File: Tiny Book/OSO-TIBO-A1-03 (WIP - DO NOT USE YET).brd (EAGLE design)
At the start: 54.9 x 88.1 mm, 106 parts, among them J2 10118193-0001LF, Q1 DMG341, Q2 IRLML0100, SW2 SPDT_SWITCH, U1 AP2112-3.3, U2 MCP73831T-2ACI/OT, U3 ATSAMD51G18A-MUT, U4 GD25Q32C, U5 MAX4468EKAT, X1 JSTPH, X2 2x5 0.05" SWD

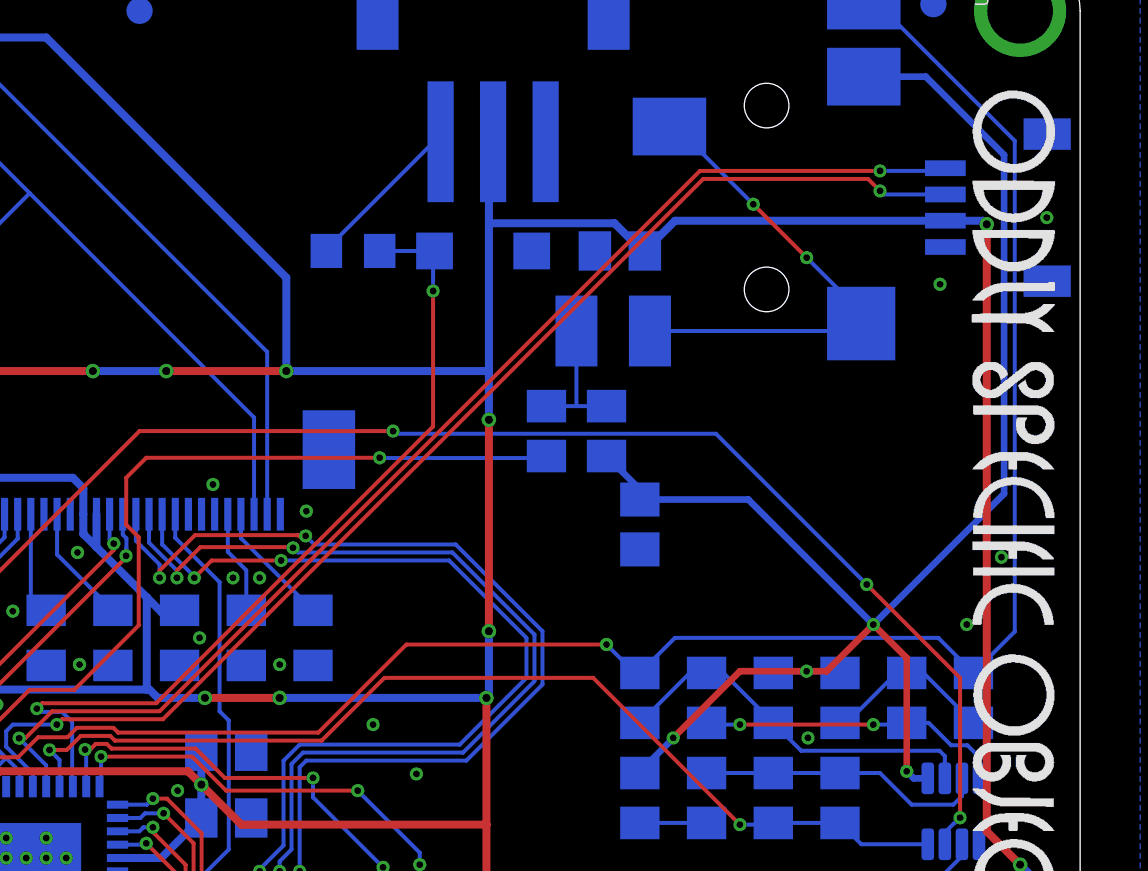
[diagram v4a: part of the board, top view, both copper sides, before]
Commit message: fix I2C routing snafu
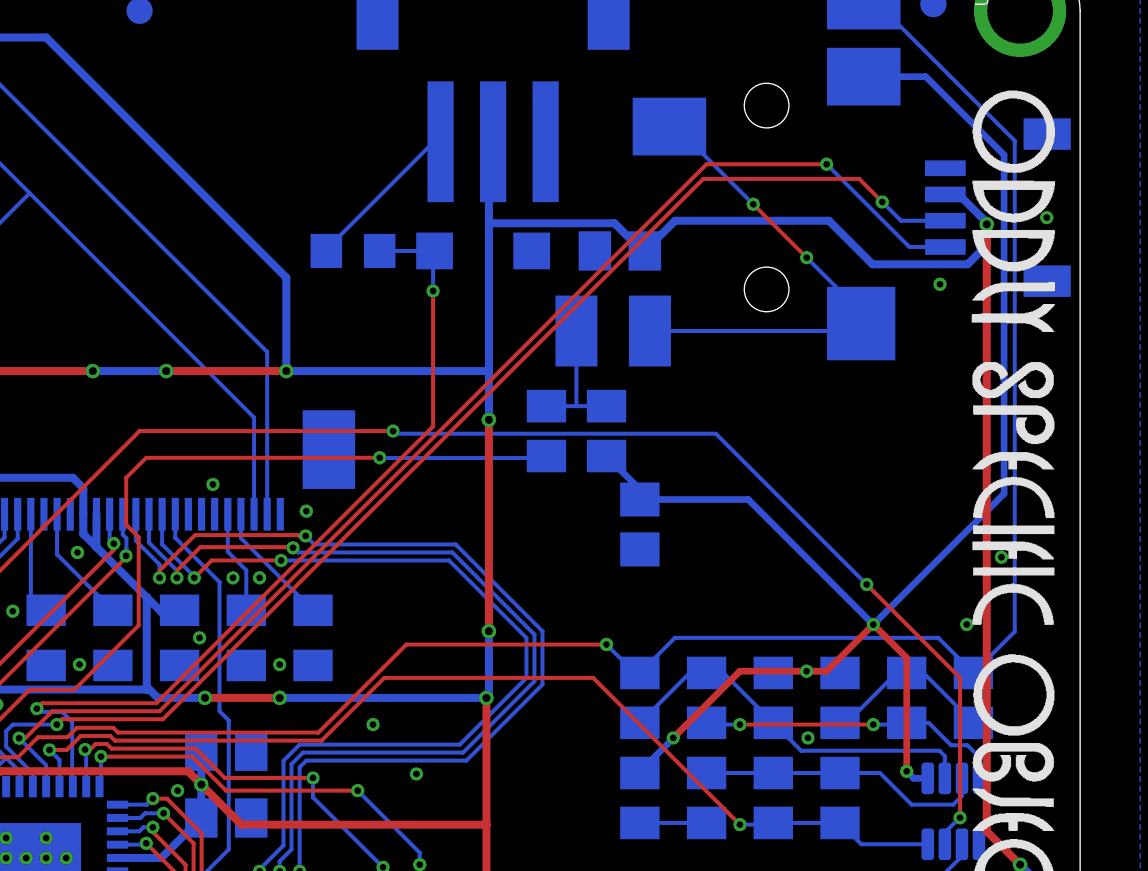
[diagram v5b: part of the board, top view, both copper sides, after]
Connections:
- net +3V3: now also I2C_PORT.2; no longer I2C_PORT.3
- net D25_SERCOM4_SDA: now also I2C_PORT.3; no longer I2C_PORT.2
- net D26_SERCOM4_SCL: now also I2C_PORT.4; no longer I2C_PORT.1
- net GND: now also I2C_PORT.1; no longer I2C_PORT.4, I2C_PORT.S1, I2C_PORT.S2
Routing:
- net +3V3: track 408.1 -> 411.9 mm
- net D26_SERCOM4_SCL: track 46.5 -> 47.9 mm
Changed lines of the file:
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@@
 <grid distance="0.01" unitdist="inch" unit="inch" style="lines" multiple="1" display="no" altdistance="0.001" altunitdist="inch" altunit="inch"/>
 <layers>
-<layer number="1" name="Top" color="4" fill="1" visible="no" active="yes"/>
+<layer number="1" name="Top" color="4" fill="1" visible="yes" active="yes"/>
 <layer number="2" name="Route2" color="1" fill="3" visible="no" active="no"/>
 <layer number="3" name="Route3" color="4" fill="3" visible="no" active="no"/>
@@
 <layer number="19" name="Unrouted" color="6" fill="1" visible="yes" active="yes"/>
 <layer number="20" name="Dimension" color="15" fill="1" visible="yes" active="yes"/>
-<layer number="21" name="tPlace" color="14" fill="1" visible="no" active="yes"/>
+<layer number="21" name="tPlace" color="14" fill="1" visible="yes" active="yes"/>
 <layer number="22" name="bPlace" color="13" fill="1" visible="yes" active="yes"/>
-<layer number="23" name="tOrigins" color="15" fill="1" visible="no" active="yes"/>
+<layer number="23" name="tOrigins" color="15" fill="1" visible="yes" active="yes"/>
 <layer number="24" name="bOrigins" color="15" fill="1" visible="yes" active="yes"/>
-<layer number="25" name="tNames" color="7" fill="1" visible="no" active="yes"/>
+<layer number="25" name="tNames" color="7" fill="1" visible="yes" active="yes"/>
 <layer number="26" name="bNames" color="7" fill="1" visible="yes" active="yes"/>
 <layer number="27" name="tValues" color="7" fill="1" visible="no" active="yes"/>
@@
 <layer number="37" name="tTest" color="7" fill="1" visible="no" active="yes"/>
 <layer number="38" name="bTest" color="7" fill="1" visible="no" active="yes"/>
-<layer number="39" name="tKeepout" color="4" fill="11" visible="no" active="yes"/>
+<layer number="39" name="tKeepout" color="4" fill="11" visible="yes" active="yes"/>
 <layer number="40" name="bKeepout" color="1" fill="11" visible="yes" active="yes"/>
-<layer number="41" name="tRestrict" color="4" fill="10" visible="no" active="yes"/>
+<layer number="41" name="tRestrict" color="4" fill="10" visible="yes" active="yes"/>
 <layer number="42" name="bRestrict" color="1" fill="10" visible="yes" active="yes"/>
 <layer number="43" name="vRestrict" color="2" fill="10" visible="no" active="yes"/>
@@
 <layer number="49" name="Reference" color="7" fill="1" visible="no" active="yes"/>
 <layer number="50" name="dxf" color="7" fill="1" visible="no" active="yes"/>
-<layer number="51" name="tDocu" color="7" fill="1" visible="no" active="yes"/>
+<layer number="51" name="tDocu" color="7" fill="1" visible="yes" active="yes"/>
 <layer number="52" name="bDocu" color="7" fill="1" visible="yes" active="yes"/>
 <layer number="53" name="tGND_GNDA" color="7" fill="9" visible="no" active="no"/>
@@
 <contactref element="U$58" pad="8"/>
 <contactref element="U$58" pad="17"/>
-<contactref element="I2C_PORT" pad="4"/>
 <contactref element="MICROSD" pad="6"/>
 <contactref element="MICROSD" pad="MT1"/>
@@
 <vertex x="48.5902" y="13.208"/>
 </polygon>
-<contactref element="I2C_PORT" pad="S1"/>
-<contactref element="I2C_PORT" pad="S2"/>
 <contactref element="R27" pad="2"/>
 <contactref element="C30" pad="2"/>
@@
 <contactref element="BTN_RESET" pad="P$1"/>
 <via x="5.8928" y="13.5636" extent="1-16" drill="0.254"/>
+<contactref element="I2C_PORT" pad="1"/>
 </signal>
 <signal name="D9_EINK_CS">
@@
 <contactref element="U$58" pad="15"/>
 <contactref element="U$58" pad="16"/>
-<contactref element="I2C_PORT" pad="3"/>
 <contactref element="MICROSD" pad="4"/>
 <contactref element="C29" pad="1"/>
@@
 <wire x1="53.274" y1="52.898" x2="53.274" y2="52.324" width="0.3048" layer="16"/>
 <via x="51.308" y="77.978" extent="1-16" drill="0.3048"/>
-<wire x1="51.308" y1="77.978" x2="51.173" y2="78.113" width="0.3048" layer="16"/>
-<wire x1="51.173" y1="78.113" x2="49.7332" y2="78.113" width="0.3048" layer="16"/>
-<wire x1="49.7332" y1="78.113" x2="39.439" y2="78.113" width="0.3048" layer="16"/>
 <wire x1="39.439" y1="78.113" x2="38.288" y2="76.962" width="0.3048" layer="16"/>
 <wire x1="32.512" y1="81.12" x2="32.35215" y2="80.96015" width="0.3048" layer="16"/>
@@
 <wire x1="5.2102" y1="60.2622" x2="3.3662" y2="60.2622" width="0.3048" layer="16"/>
 <wire x1="3.3662" y1="60.2622" x2="3.302" y2="60.198" width="0.3048" layer="16"/>
+<contactref element="I2C_PORT" pad="2"/>
+<wire x1="49.7332" y1="79.113" x2="50.23925" y2="79.113" width="0.3048" layer="16"/>
+<wire x1="51.308" y1="78.04425" x2="50.23925" y2="79.113" width="0.3048" layer="16"/>
+<wire x1="51.308" y1="78.04425" x2="51.308" y2="77.978" width="0.3048" layer="16"/>
+<wire x1="51.308" y1="77.978" x2="51.308" y2="77.18175" width="0.3048" layer="16"/>
+<wire x1="51.308" y1="77.18175" x2="50.58025" y2="76.454" width="0.3048" layer="16"/>
+<wire x1="45.30018125" y1="78.113" x2="39.439" y2="78.113" width="0.3048" layer="16"/>
+<wire x1="46.95918125" y1="76.454" x2="45.30018125" y2="78.113" width="0.3048" layer="16"/>
+<wire x1="50.58025" y1="76.454" x2="46.95918125" y2="76.454" width="0.3048" layer="16"/>
 </signal>
 <signal name="GDR">
@@
 <signal name="D25_SERCOM4_SDA">
 <contactref element="U3" pad="7"/>
-<contactref element="I2C_PORT" pad="2"/>
 <via x="15.9004" y="58.928" extent="1-16" drill="0.254"/>
-<wire x1="40.513" y1="79.7052" x2="46.7868" y2="79.7052" width="0.1524" layer="1"/>
-<wire x1="46.7868" y1="79.7052" x2="47.244" y2="79.248" width="0.1524" layer="1"/>
-<via x="47.244" y="79.248" extent="1-16" drill="0.254"/>
-<wire x1="47.244" y1="79.248" x2="47.379" y2="79.113" width="0.1524" layer="16"/>
-<wire x1="47.379" y1="79.113" x2="49.7332" y2="79.113" width="0.1524" layer="16"/>
 <wire x1="40.513" y1="79.7052" x2="19.939" y2="59.1312" width="0.1524" layer="1"/>
 <wire x1="14.986" y1="56.5658" x2="14.986" y2="57.0738" width="0.1524" layer="16"/>
@@
 <wire x1="16.1036" y1="59.1312" x2="15.9004" y2="58.928" width="0.1524" layer="1"/>
 <wire x1="19.939" y1="59.1312" x2="16.1036" y2="59.1312" width="0.1524" layer="1"/>
+<contactref element="I2C_PORT" pad="3"/>
+<wire x1="49.7332" y1="78.113" x2="48.0455" y2="78.113" width="0.1524" layer="16"/>
+<wire x1="48.0455" y1="78.113" x2="47.33125" y2="78.82725" width="0.1524" layer="16"/>
+<via x="47.33125" y="78.82725" extent="1-16" drill="0.254"/>
+<wire x1="47.33125" y1="78.82725" x2="46.4533" y2="79.7052" width="0.1524" layer="1"/>
+<wire x1="46.4533" y1="79.7052" x2="40.513" y2="79.7052" width="0.1524" layer="1"/>
 </signal>
 <signal name="D26_SERCOM4_SCL">
 <contactref element="U3" pad="8"/>
-<contactref element="I2C_PORT" pad="1"/>
-<wire x1="49.7332" y1="80.113" x2="49.6302" y2="80.01" width="0.1524" layer="16"/>
-<wire x1="49.6302" y1="80.01" x2="47.244" y2="80.01" width="0.1524" layer="16"/>
-<via x="47.244" y="80.01" extent="1-16" drill="0.254"/>
-<wire x1="40.386" y1="80.01" x2="47.244" y2="80.01" width="0.1524" layer="1"/>
+<wire x1="40.64" y1="80.264" x2="45.212" y2="80.264" width="0.1524" layer="1"/>
 <via x="14.46365" y="58.40895" extent="1-16" drill="0.254"/>
 <wire x1="15.494" y1="57.3786" x2="14.46365" y2="58.40895" width="0.1524" layer="16"/>
@@
 <wire x1="14.46365" y1="58.40895" x2="14.69555" y2="58.40895" width="0.1524" layer="1"/>
 <wire x1="15.7226" y1="59.436" x2="19.812" y2="59.436" width="0.1524" layer="1"/>
-<wire x1="19.812" y1="59.436" x2="40.386" y2="80.01" width="0.1524" layer="1"/>
+<wire x1="19.812" y1="59.436" x2="40.64" y2="80.264" width="0.1524" layer="1"/>
+<contactref element="I2C_PORT" pad="4"/>
+<wire x1="49.7332" y1="77.113" x2="48.363" y2="77.113" width="0.1524" layer="16"/>
+<wire x1="48.363" y1="77.113" x2="45.212" y2="80.264" width="0.1524" layer="16"/>
+<via x="45.212" y="80.264" extent="1-16" drill="0.254"/>
 </signal>
 <signal name="D28_SERCOM5_MOSI">
